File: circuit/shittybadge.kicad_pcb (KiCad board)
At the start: 2 copper layers, 39 parts, among them J1 USB_B_Micro, J2 E8124-015-01, J4 B4B-PH-K-S_LF__SN_, U1 CP2102N-A01-GQFN24, U2 STUSB4500QTR, U3 LMZM23601V3, U4 ESP-12E, U5 LMZM23601V5, U6 myDisplay

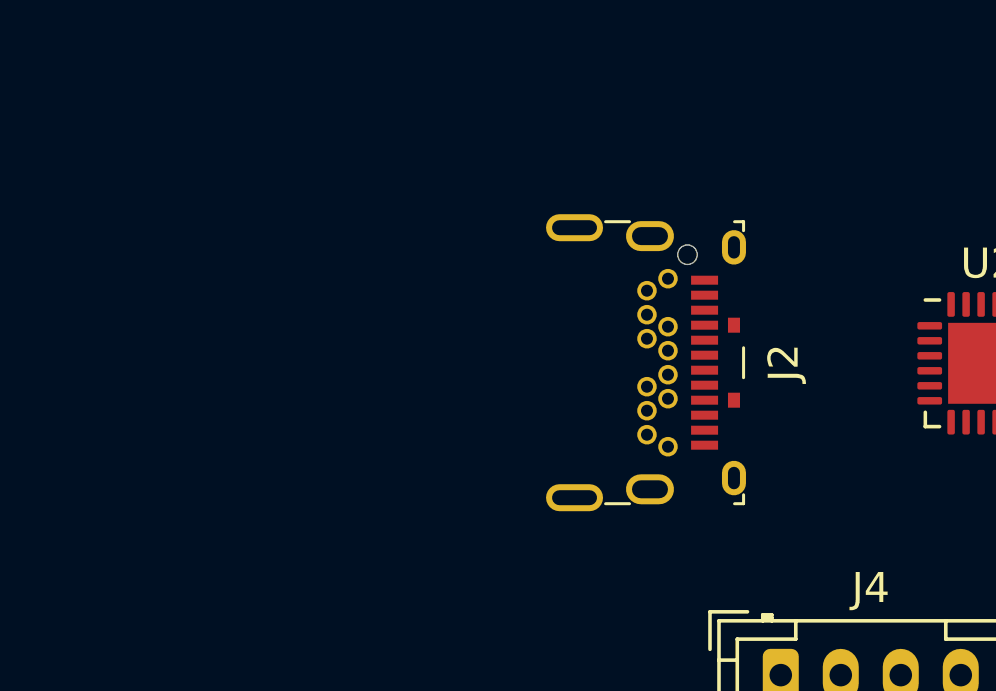
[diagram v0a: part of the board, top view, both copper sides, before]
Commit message: changed usbc to usb2
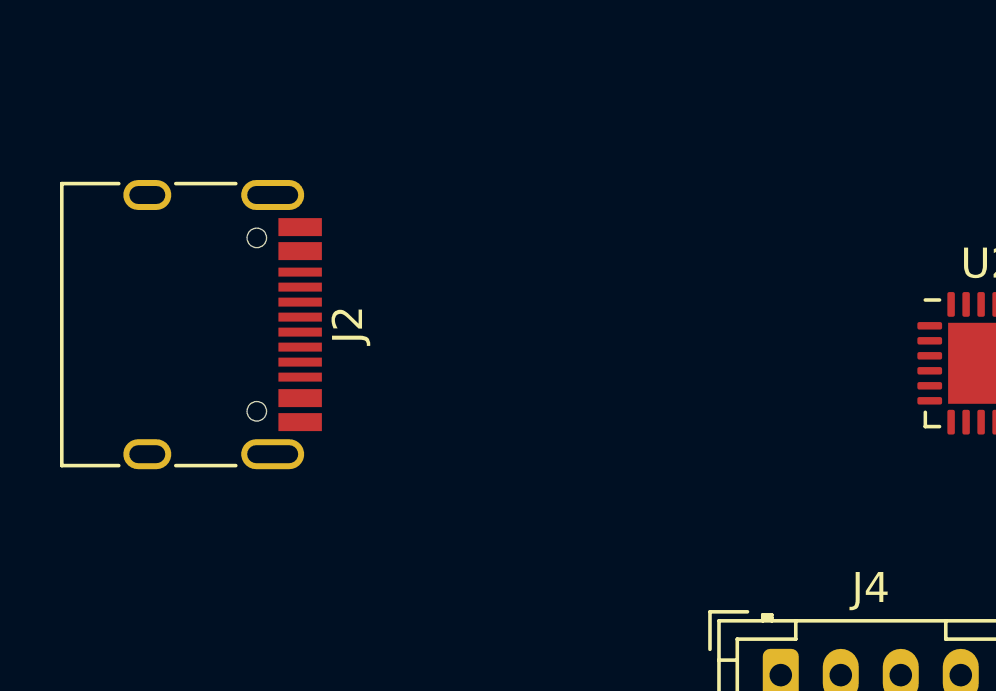
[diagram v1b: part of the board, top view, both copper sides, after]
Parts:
- J2: footprint digikey-footprints:USB-C_Female_E8124-015-01 -> Connector_USB:USB_C_Receptacle_HRO_TYPE-C-31-M-12
- moved J2 17.6 mm to (101.6, 140.0)

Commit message: did some routing
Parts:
- added R13: 10k, Resistor_SMD:R_1206_3216Metric_Pad1.42x1.75mm_HandSolder, F.Cu at (114.0, 85.3)
- added R14: 10k, Resistor_SMD:R_1206_3216Metric_Pad1.42x1.75mm_HandSolder, F.Cu at (138.2, 104.4)
- added S2: pts647, mylibrary:pts647, F.Cu at (144.5, 108.2)
- moved D4 92.4 mm to (117.6, 73.2), turned to 180 degrees
- moved D3 80.9 mm to (133.3, 73.2), turned to 180 degrees
- moved U3 74.8 mm to (116.3, 78.0), turned to 0 degrees
- moved D2 74.8 mm to (107.4, 104.6)
- moved R5 66.8 mm to (111.5, 93.2)
- moved U5 66.1 mm to (132.0, 78.0), turned to 0 degrees
- moved R6 65.7 mm to (111.5, 90.7), turned to 180 degrees
- moved C13 65.6 mm to (118.4, 69.1), turned to 180 degrees
- moved C5 63.7 mm to (112.3, 78.7), turned to 90 degrees
- moved R8 61.9 mm to (115.6, 93.0), turned to 90 degrees
- moved C9 61.8 mm to (120.7, 78.7), turned to 90 degrees
- moved R7 57.1 mm to (113.0, 104.1), turned to 270 degrees
- moved J1 55.4 mm to (156.7, 95.8), turned to 90 degrees
- moved R4 54.6 mm to (111.5, 95.8), turned to 180 degrees
- moved U1 54.5 mm to (139.3, 92.7), turned to 90 degrees
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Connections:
- D1 pad 4: Net-(D1-Pad4) -> Net-(C1-Pad2)
- J1 pad 2: Net-(D1-Pad2) -> Net-(D1-Pad3)
- J1 pad 3: Net-(D1-Pad3) -> Net-(D1-Pad2)
- R1 pad 1: Net-(D1-Pad4) -> Net-(R1-Pad1)
- R2 pad 1: Net-(D1-Pad4) -> Net-(R1-Pad1)
- S1 pad 1: GND -> Net-(R12-Pad2)
- S1 pad 3: Net-(R12-Pad2) -> GND
- U1 pad 19: (no net) -> Net-(R13-Pad1)
- U1 pad 23: (no net) -> Net-(R12-Pad2)
- U1 pad 3: Net-(D1-Pad3) -> Net-(D1-Pad2)
- U1 pad 4: Net-(D1-Pad2) -> Net-(D1-Pad3)
- U1 pad 8: Net-(D1-Pad4) -> Net-(R1-Pad1)
- U4 pad 1: (no net) -> Net-(R13-Pad1)
- U4 pad 16: GND -> Net-(R14-Pad1)
- U4 pad 17: (no net) -> Net-(S2-Pad1)
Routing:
- net Net-(R13-Pad1): track 0.00 -> 19.7 mm
- net GND: track 0.00 -> 16.9 mm
- net Net-(C2-Pad1): track 0.00 -> 14.9 mm
- net Net-(R12-Pad2): track 0.00 -> 12.6 mm
- net Net-(R1-Pad1): track 0.00 -> 5.72 mm
- net Net-(U1-Pad20): track 0.00 -> 4.01 mm
- net Net-(U1-Pad21): track 0.00 -> 3.63 mm
- net Net-(R3-Pad2): track 0.00 -> 2.75 mm
- net Net-(C1-Pad2): track 0.00 -> 1.54 mm
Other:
- board outline added: 65.3 x 51.6 mm
- rule pad_to_mask_clearance: 0.05 -> 0.051
- rule trace_min: 0.2 -> 0.127

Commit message: continued routing
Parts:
- moved J1 2.05 mm to (156.5, 97.8)
- moved C4 1.35 mm to (150.4, 98.0)
- moved R2 1.01 mm to (146.8, 93.7)
- moved C1 0.59 mm to (152.1, 99.6)
- moved D1 0.53 mm to (151.6, 94.7)
- moved R1 0.45 mm to (143.3, 94.2), turned to 270 degrees
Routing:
- net GND: track 16.9 -> 152.8 mm, vias 0 -> 5
- net SCL: track 0.00 -> 54.5 mm, vias 0 -> 2
- net SDA: track 0.00 -> 50.3 mm, vias 0 -> 2
- net VBUS: track 0.00 -> 28.9 mm
- net +3V3: track 0.00 -> 25.3 mm
- net ALERT_PD: track 0.00 -> 24.1 mm
- net Net-(D1-Pad2): track 0.00 -> 21.5 mm, vias 0 -> 2
- net RST_PD: track 0.00 -> 16.6 mm, vias 0 -> 2
- net Net-(R12-Pad2): track 12.6 -> 27.4 mm
- net ATTACH_PD: track 0.00 -> 14.7 mm
- net Net-(D1-Pad3): track 0.00 -> 12.4 mm
- net Net-(S2-Pad1): track 0.00 -> 11.5 mm
- net Net-(C1-Pad2): track 1.54 -> 10.2 mm
- net Net-(R4-Pad1): track 0.00 -> 6.01 mm
- net Net-(R14-Pad1): track 0.00 -> 4.42 mm
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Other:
- outline, holes or cut-outs redrawn

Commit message: done routing v1
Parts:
- moved S1 8.00 mm to (142.8, 106.2), turned to 270 degrees
- moved S2 6.06 mm to (142.8, 114.0), turned to 270 degrees
- moved R13 1.02 mm to (114.4, 86.3)
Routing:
- net GND: track 152.8 -> 311.2 mm, vias 5 -> 7
- net +3V3: track 25.3 -> 84.6 mm, vias 0 -> 3
- net VBUS: track 28.9 -> 86.6 mm, vias 0 -> 4
- net +5V: track 0.00 -> 43.9 mm, vias 0 -> 3
- net Net-(D3-Pad2): track 0.00 -> 39.4 mm, vias 0 -> 4
- net Net-(D3-Pad4): track 0.00 -> 32.9 mm, vias 0 -> 2
- net Net-(R8-Pad2): track 0.00 -> 14.9 mm
- net Net-(S2-Pad1): track 11.5 -> 23.3 mm
- net Net-(C1-Pad2): track 10.2 -> 18.4 mm, vias 0 -> 2
- net Net-(D1-Pad3): track 12.4 -> 18.9 mm, vias 0 -> 2
- net Net-(R5-Pad2): track 2.54 -> 8.38 mm
- net Net-(R13-Pad1): track 19.7 -> 25.3 mm
- net Net-(R12-Pad2): track 27.4 -> 23.5 mm
- net Net-(R8-Pad1): track 0.00 -> 3.19 mm
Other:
- outline, holes or cut-outs redrawn

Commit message: ordering
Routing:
- net GND: track 311.2 -> 315.3 mm, vias 7 -> 5
- added copper zone on B.Cu, net GND
- added copper zone on B.Cu, net VBUS
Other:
- board text added: "JLCJLCJLCJLC"
